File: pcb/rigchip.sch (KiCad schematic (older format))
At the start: 28 parts, among them IC1 TSR1, IC2 CHIPv1_0, J1 POWER, J2 DATA, J3 CONTROL

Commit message: first go at routing
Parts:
- J1: footprint (none) -> agg:S02B-PASK-2
- J2: footprint (none) -> agg:S05B-PASK-2
- J3: footprint (none) -> agg:S03B-PASK-2
- L1: value 5.6µ -> 6µ8; footprint (none) -> agg:TYS5040; Farnell (none) -> 2292530
- L2, L3, L4, L5, L6, L7: value L -> FB
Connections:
- net GND: now also IC2.L1 (GND)
- net at IC2.R15 (XIO-P2): now also R1.1
- net at IC2.R16 (XIO-P3): now also R2.1
- net at IC2.R19 (XIO-P6): no longer R1.1
- net at IC2.R20 (XIO-P7): no longer R2.1
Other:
- moved on the sheet: D8, D9, R1, R2

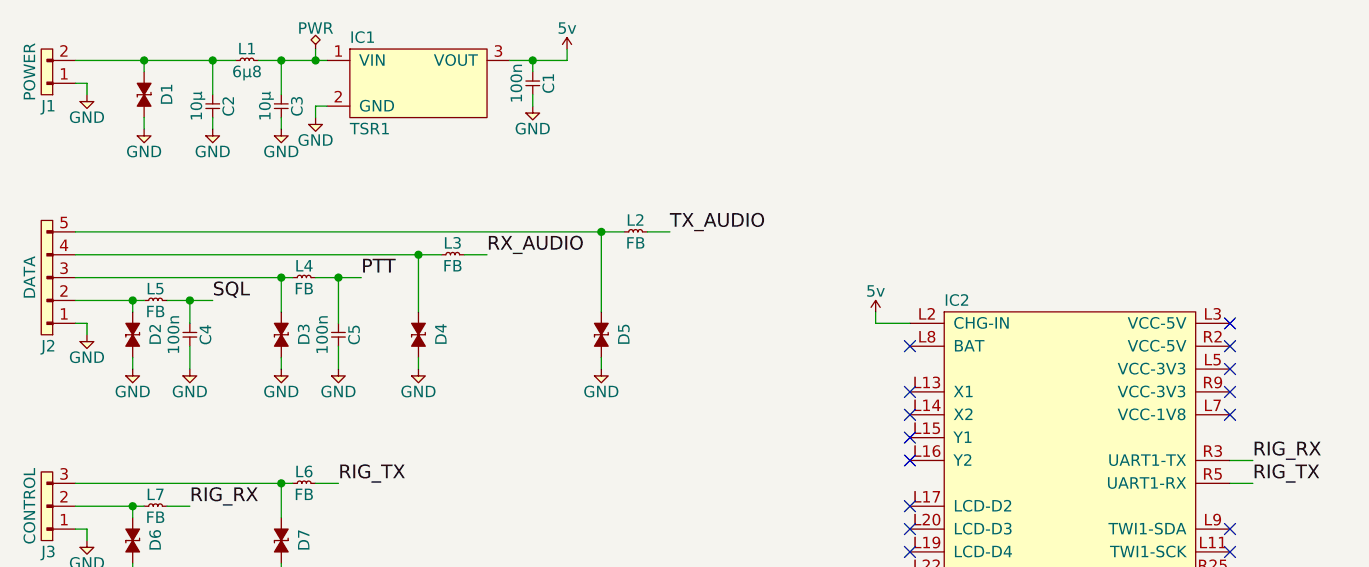
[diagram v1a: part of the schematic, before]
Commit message: reroute, no more tracks underneath and nice shielding
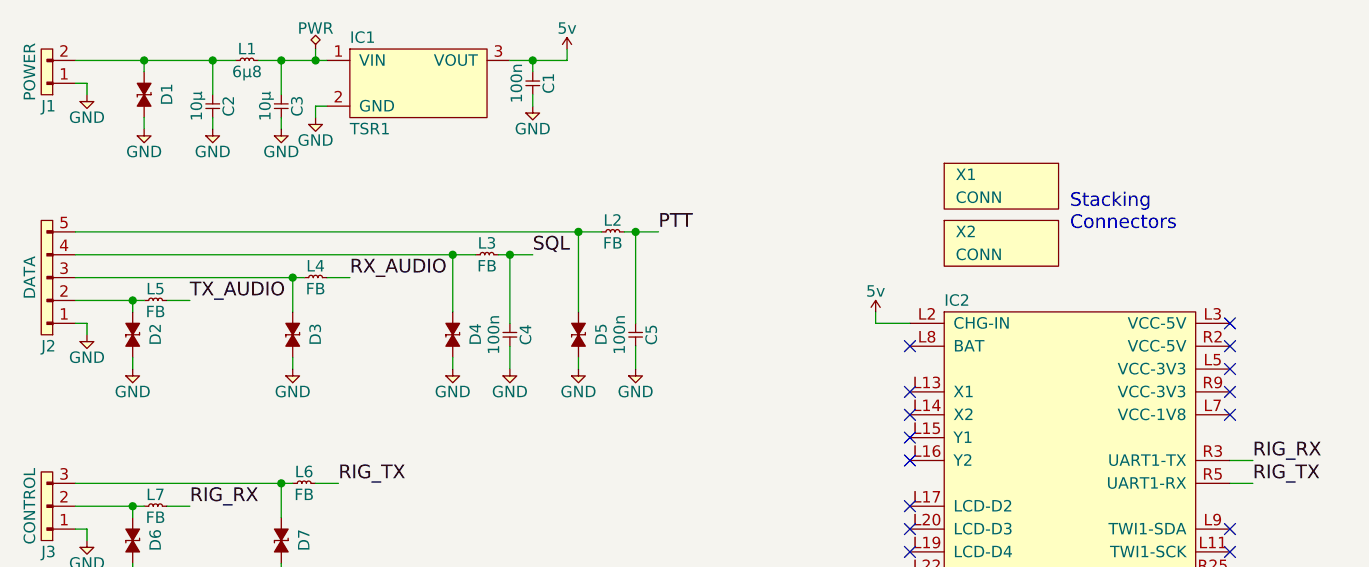
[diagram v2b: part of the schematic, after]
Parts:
- added X1, X2: CONN, symbol PART
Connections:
- net PTT: now also L2.2; no longer L4.2
- net RX_AUDIO: now also L4.2; no longer L3.2
- net SQL: now also L3.2; no longer L5.2
- net TX_AUDIO: now also L5.2; no longer L2.2
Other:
- note added: "Stacking\nConnectors"
- moved on the sheet: C4, C5, D3, D4, D5, L2, L3, L4
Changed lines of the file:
@@
 L ESD_DIODE D5
 U 1 1 56F7F170
-P 3450 2100
-F 0 "D5" H 3400 2200 50  0000 L CNN
-F 1 "ESD_DIODE" H 3400 2000 50  0001 L CNN
-F 2 "agg:0402" H 3400 1900 50  0001 L CNN
-F 3 "" H 3350 2100 50  0001 C CNN
-F 4 "2368169" H 3400 1800 50  0001 L CNN "Farnell"
-	1    3450 2100
+P 3350 2100
+F 0 "D5" H 3300 2200 50  0000 L CNN
+F 1 "ESD_DIODE" H 3300 2000 50  0001 L CNN
+F 2 "agg:0402" H 3300 1900 50  0001 L CNN
+F 3 "" H 3250 2100 50  0001 C CNN
+F 4 "2368169" H 3300 1800 50  0001 L CNN "Farnell"
+	1    3350 2100
 	0    1    1    0
 $EndComp
@@
 L ESD_DIODE D4
 U 1 1 56F7F1C6
-P 2650 2100
-F 0 "D4" H 2600 2200 50  0000 L CNN
-F 1 "ESD_DIODE" H 2600 2000 50  0001 L CNN
-F 2 "agg:0402" H 2600 1900 50  0001 L CNN
-F 3 "" H 2550 2100 50  0001 C CNN
-F 4 "2368169" H 2600 1800 50  0001 L CNN "Farnell"
-	1    2650 2100
+P 2800 2100
+F 0 "D4" H 2750 2200 50  0000 L CNN
+F 1 "ESD_DIODE" H 2750 2000 50  0001 L CNN
+F 2 "agg:0402" H 2750 1900 50  0001 L CNN
+F 3 "" H 2700 2100 50  0001 C CNN
+F 4 "2368169" H 2750 1800 50  0001 L CNN "Farnell"
+	1    2800 2100
 	0    1    1    0
 $EndComp
@@
 L ESD_DIODE D3
 U 1 1 56F7F1FF
-P 2050 2100
-F 0 "D3" H 2000 2200 50  0000 L CNN
-F 1 "ESD_DIODE" H 2000 2000 50  0001 L CNN
-F 2 "agg:0402" H 2000 1900 50  0001 L CNN
-F 3 "" H 1950 2100 50  0001 C CNN
-F 4 "2368169" H 2000 1800 50  0001 L CNN "Farnell"
-	1    2050 2100
+P 2100 2100
+F 0 "D3" H 2050 2200 50  0000 L CNN
+F 1 "ESD_DIODE" H 2050 2000 50  0001 L CNN
+F 2 "agg:0402" H 2050 1900 50  0001 L CNN
+F 3 "" H 2000 2100 50  0001 C CNN
+F 4 "2368169" H 2050 1800 50  0001 L CNN "Farnell"
+	1    2100 2100
 	0    1    1    0
 $EndComp
@@
 L C C4
 U 1 1 56F7F528
-P 1650 2050
-F 0 "C4" H 1700 2120 50  0000 C CNN
-F 1 "100n" H 1700 1980 50  0000 C CNN
-F 2 "agg:0603" H 1650 2050 50  0001 C CNN
-F 3 "" H 1650 2050 50  0001 C CNN
-	1    1650 2050
+P 3050 2050
+F 0 "C4" H 3100 2120 50  0000 C CNN
+F 1 "100n" H 3100 1980 50  0000 C CNN
+F 2 "agg:0603" H 3050 2050 50  0001 C CNN
+F 3 "" H 3050 2050 50  0001 C CNN
+	1    3050 2050
 	0    1    1    0
 $EndComp
@@
 L C C5
 U 1 1 56F7F59B
-P 2300 2050
-F 0 "C5" H 2350 2120 50  0000 C CNN
-F 1 "100n" H 2350 1980 50  0000 C CNN
-F 2 "agg:0603" H 2300 2050 50  0001 C CNN
-F 3 "" H 2300 2050 50  0001 C CNN
-	1    2300 2050
+P 3600 2050
+F 0 "C5" H 3650 2120 50  0000 C CNN
+F 1 "100n" H 3650 1980 50  0000 C CNN
+F 2 "agg:0603" H 3600 2050 50  0001 C CNN
+F 3 "" H 3600 2050 50  0001 C CNN
+	1    3600 2050
 	0    1    1    0
 $EndComp
@@
 L GND #PWR010
 U 1 1 56F826D2
-P 2050 2250
-F 0 "#PWR010" H 1920 2290 50  0001 L CNN
-F 1 "GND" H 2050 2150 50  0000 C CNN
-F 2 "" H 2050 2250 60  0000 C CNN
-F 3 "" H 2050 2250 60  0000 C CNN
-	1    2050 2250
+P 2100 2250
+F 0 "#PWR010" H 1970 2290 50  0001 L CNN
+F 1 "GND" H 2100 2150 50  0000 C CNN
+F 2 "" H 2100 2250 60  0000 C CNN
+F 3 "" H 2100 2250 60  0000 C CNN
+	1    2100 2250
 	1    0    0    -1
 $EndComp
@@
 L GND #PWR011
 U 1 1 56F82716
-P 2650 2250
-F 0 "#PWR011" H 2520 2290 50  0001 L CNN
-F 1 "GND" H 2650 2150 50  0000 C CNN
-F 2 "" H 2650 2250 60  0000 C CNN
-F 3 "" H 2650 2250 60  0000 C CNN
-	1    2650 2250
+P 2800 2250
+F 0 "#PWR011" H 2670 2290 50  0001 L CNN
+F 1 "GND" H 2800 2150 50  0000 C CNN
+F 2 "" H 2800 2250 60  0000 C CNN
+F 3 "" H 2800 2250 60  0000 C CNN
+	1    2800 2250
 	1    0    0    -1
 $EndComp
@@
 L GND #PWR012
 U 1 1 56F8275A
-P 3450 2250
-F 0 "#PWR012" H 3320 2290 50  0001 L CNN
-F 1 "GND" H 3450 2150 50  0000 C CNN
-F 2 "" H 3450 2250 60  0000 C CNN
-F 3 "" H 3450 2250 60  0000 C CNN
-	1    3450 2250
+P 3350 2250
+F 0 "#PWR012" H 3220 2290 50  0001 L CNN
+F 1 "GND" H 3350 2150 50  0000 C CNN
+F 2 "" H 3350 2250 60  0000 C CNN
+F 3 "" H 3350 2250 60  0000 C CNN
+	1    3350 2250
 	1    0    0    -1
 $EndComp
@@
 L GND #PWR013
 U 1 1 56F829A6
-P 1650 2250
-F 0 "#PWR013" H 1520 2290 50  0001 L CNN
-F 1 "GND" H 1650 2150 50  0000 C CNN
-F 2 "" H 1650 2250 60  0000 C CNN
-F 3 "" H 1650 2250 60  0000 C CNN
-	1    1650 2250
+P 3050 2250
+F 0 "#PWR013" H 2920 2290 50  0001 L CNN
+F 1 "GND" H 3050 2150 50  0000 C CNN
+F 2 "" H 3050 2250 60  0000 C CNN
+F 3 "" H 3050 2250 60  0000 C CNN
+	1    3050 2250
 	1    0    0    -1
 $EndComp
@@
 L GND #PWR014
 U 1 1 56F829EA
-P 2300 2250
-F 0 "#PWR014" H 2170 2290 50  0001 L CNN
-F 1 "GND" H 2300 2150 50  0000 C CNN
-F 2 "" H 2300 2250 60  0000 C CNN
-F 3 "" H 2300 2250 60  0000 C CNN
-	1    2300 2250
+P 3600 2250
+F 0 "#PWR014" H 3470 2290 50  0001 L CNN
+F 1 "GND" H 3600 2150 50  0000 C CNN
+F 2 "" H 3600 2250 60  0000 C CNN
+F 3 "" H 3600 2250 60  0000 C CNN
+	1    3600 2250
 	1    0    0    -1
 $EndComp
@@
 L L L4
 U 1 1 56F82B65
-P 2100 1850
-F 0 "L4" H 2150 1900 50  0000 C CNN
-F 1 "FB" H 2150 1800 50  0000 C CNN
-F 2 "agg:0603" H 2100 1850 50  0001 C CNN
-F 3 "" H 2100 1850 50  0001 C CNN
-	1    2100 1850
+P 2150 1850
+F 0 "L4" H 2200 1900 50  0000 C CNN
+F 1 "FB" H 2200 1800 50  0000 C CNN
+F 2 "agg:0603" H 2150 1850 50  0001 C CNN
+F 3 "" H 2150 1850 50  0001 C CNN
+	1    2150 1850
 	1    0    0    -1
 $EndComp
@@
 L L L3
 U 1 1 56F82BD1
-P 2750 1750
-F 0 "L3" H 2800 1800 50  0000 C CNN
-F 1 "FB" H 2800 1700 50  0000 C CNN
-F 2 "agg:0603" H 2750 1750 50  0001 C CNN
-F 3 "" H 2750 1750 50  0001 C CNN
-	1    2750 1750
+P 2900 1750
+F 0 "L3" H 2950 1800 50  0000 C CNN
+F 1 "FB" H 2950 1700 50  0000 C CNN
+F 2 "agg:0603" H 2900 1750 50  0001 C CNN
+F 3 "" H 2900 1750 50  0001 C CNN
+	1    2900 1750
 	1    0    0    -1
 $EndComp
@@
 L L L2
 U 1 1 56F82C32
-P 3550 1650
-F 0 "L2" H 3600 1700 50  0000 C CNN
-F 1 "FB" H 3600 1600 50  0000 C CNN
-F 2 "agg:0603" H 3550 1650 50  0001 C CNN
-F 3 "" H 3550 1650 50  0001 C CNN
-	1    3550 1650
-	1    0    0    -1
-$EndComp
-Text Label 1750 1950 0    60   ~ 0
+P 3450 1650
+F 0 "L2" H 3500 1700 50  0000 C CNN
+F 1 "FB" H 3500 1600 50  0000 C CNN
+F 2 "agg:0603" H 3450 1650 50  0001 C CNN
+F 3 "" H 3450 1650 50  0001 C CNN
+	1    3450 1650
+	1    0    0    -1
+$EndComp
+Text Label 3150 1750 0    60   ~ 0
 SQL
-Text Label 2400 1850 0    60   ~ 0
+Text Label 3700 1650 0    60   ~ 0
 PTT
-Text Label 2950 1750 0    60   ~ 0
+Text Label 2350 1850 0    60   ~ 0
 RX_AUDIO
-Text Label 3750 1650 0    60   ~ 0
+Text Label 1650 1950 0    60   ~ 0
 TX_AUDIO
 $Comp
@@
 Connection ~ 1400 1950
 Wire Wire Line
-	1550 1950 1750 1950
-Wire Wire Line
-	1650 1950 1650 2050
-Wire Wire Line
-	1650 2150 1650 2250
+	3050 1750 3050 2050
+Wire Wire Line
+	3050 2150 3050 2250
 Wire Wire Line
 	1400 2200 1400 2250
-Connection ~ 1650 1950
-Wire Wire Line
-	1150 1850 2100 1850
-Wire Wire Line
-	2050 1850 2050 2000
-Connection ~ 2050 1850
-Wire Wire Line
-	2050 2200 2050 2250
-Wire Wire Line
-	2300 2250 2300 2150
-Wire Wire Line
-	2200 1850 2400 1850
-Wire Wire Line
-	2300 1850 2300 2050
-Connection ~ 2300 1850
-Wire Wire Line
-	1150 1750 2750 1750
-Wire Wire Line
-	2650 2200 2650 2250
-Wire Wire Line
-	3450 2200 3450 2250
-Wire Wire Line
-	1150 1650 3550 1650
+Wire Wire Line
+	1150 1850 2150 1850
+Wire Wire Line
+	2100 1850 2100 2000
+Connection ~ 2100 1850
+Wire Wire Line
+	2100 2200 2100 2250
+Wire Wire Line
+	3600 2250 3600 2150
+Wire Wire Line
+	3600 1650 3600 2050
+Wire Wire Line
+	1150 1750 2900 1750
+Wire Wire Line
+	2800 2200 2800 2250
+Wire Wire Line
+	3350 2200 3350 2250
 Wire Wire Line
 	1150 2950 1200 2950
@@
 	1400 2850 1400 2900
 Wire Wire Line
-	2650 1750 2650 2000
-Connection ~ 2650 1750
-Wire Wire Line
-	2850 1750 2950 1750
-Wire Wire Line
-	3450 1650 3450 2000
-Connection ~ 3450 1650
-Wire Wire Line
-	3750 1650 3650 1650
+	2800 1750 2800 2000
+Connection ~ 2800 1750
+Wire Wire Line
+	3000 1750 3150 1750
+Wire Wire Line
+	3350 1650 3350 2000
+Connection ~ 3350 1650
+Wire Wire Line
+	3550 1650 3700 1650
 Connection ~ 1400 2850
 Wire Wire Line
@@
 NoConn ~ 6200 4050
 NoConn ~ 6200 4150
+$Comp
+L PART X1
+U 1 1 56F82D3C
+P 4950 1500
+F 0 "X1" H 5000 1600 50  0000 L CNN
+F 1 "CONN" H 5000 1500 50  0000 L CNN
+F 2 "" H 4950 1500 50  0001 C CNN
+F 3 "" H 4950 1500 50  0001 C CNN
+F 4 "1569230" H 4950 1500 60  0001 C CNN "Farnell"
+	1    4950 1500
+	1    0    0    -1
+$EndComp
+$Comp
+L PART X2
+U 1 1 56F82E20
+P 4950 1750
+F 0 "X2" H 5000 1850 50  0000 L CNN
+F 1 "CONN" H 5000 1750 50  0000 L CNN
+F 2 "" H 4950 1750 50  0001 C CNN
+F 3 "" H 4950 1750 50  0001 C CNN
+F 4 "1569230" H 4950 1750 60  0001 C CNN "Farnell"
+	1    4950 1750
+	1    0    0    -1
+$EndComp
+Text Notes 5500 1650 0    60   ~ 0
+Stacking\nConnectors
+Wire Wire Line
+	1550 1950 1650 1950
+Wire Wire Line
+	2350 1850 2250 1850
+Connection ~ 3050 1750
+Wire Wire Line
+	1150 1650 3450 1650
+Connection ~ 3600 1650
 $EndSCHEMATC

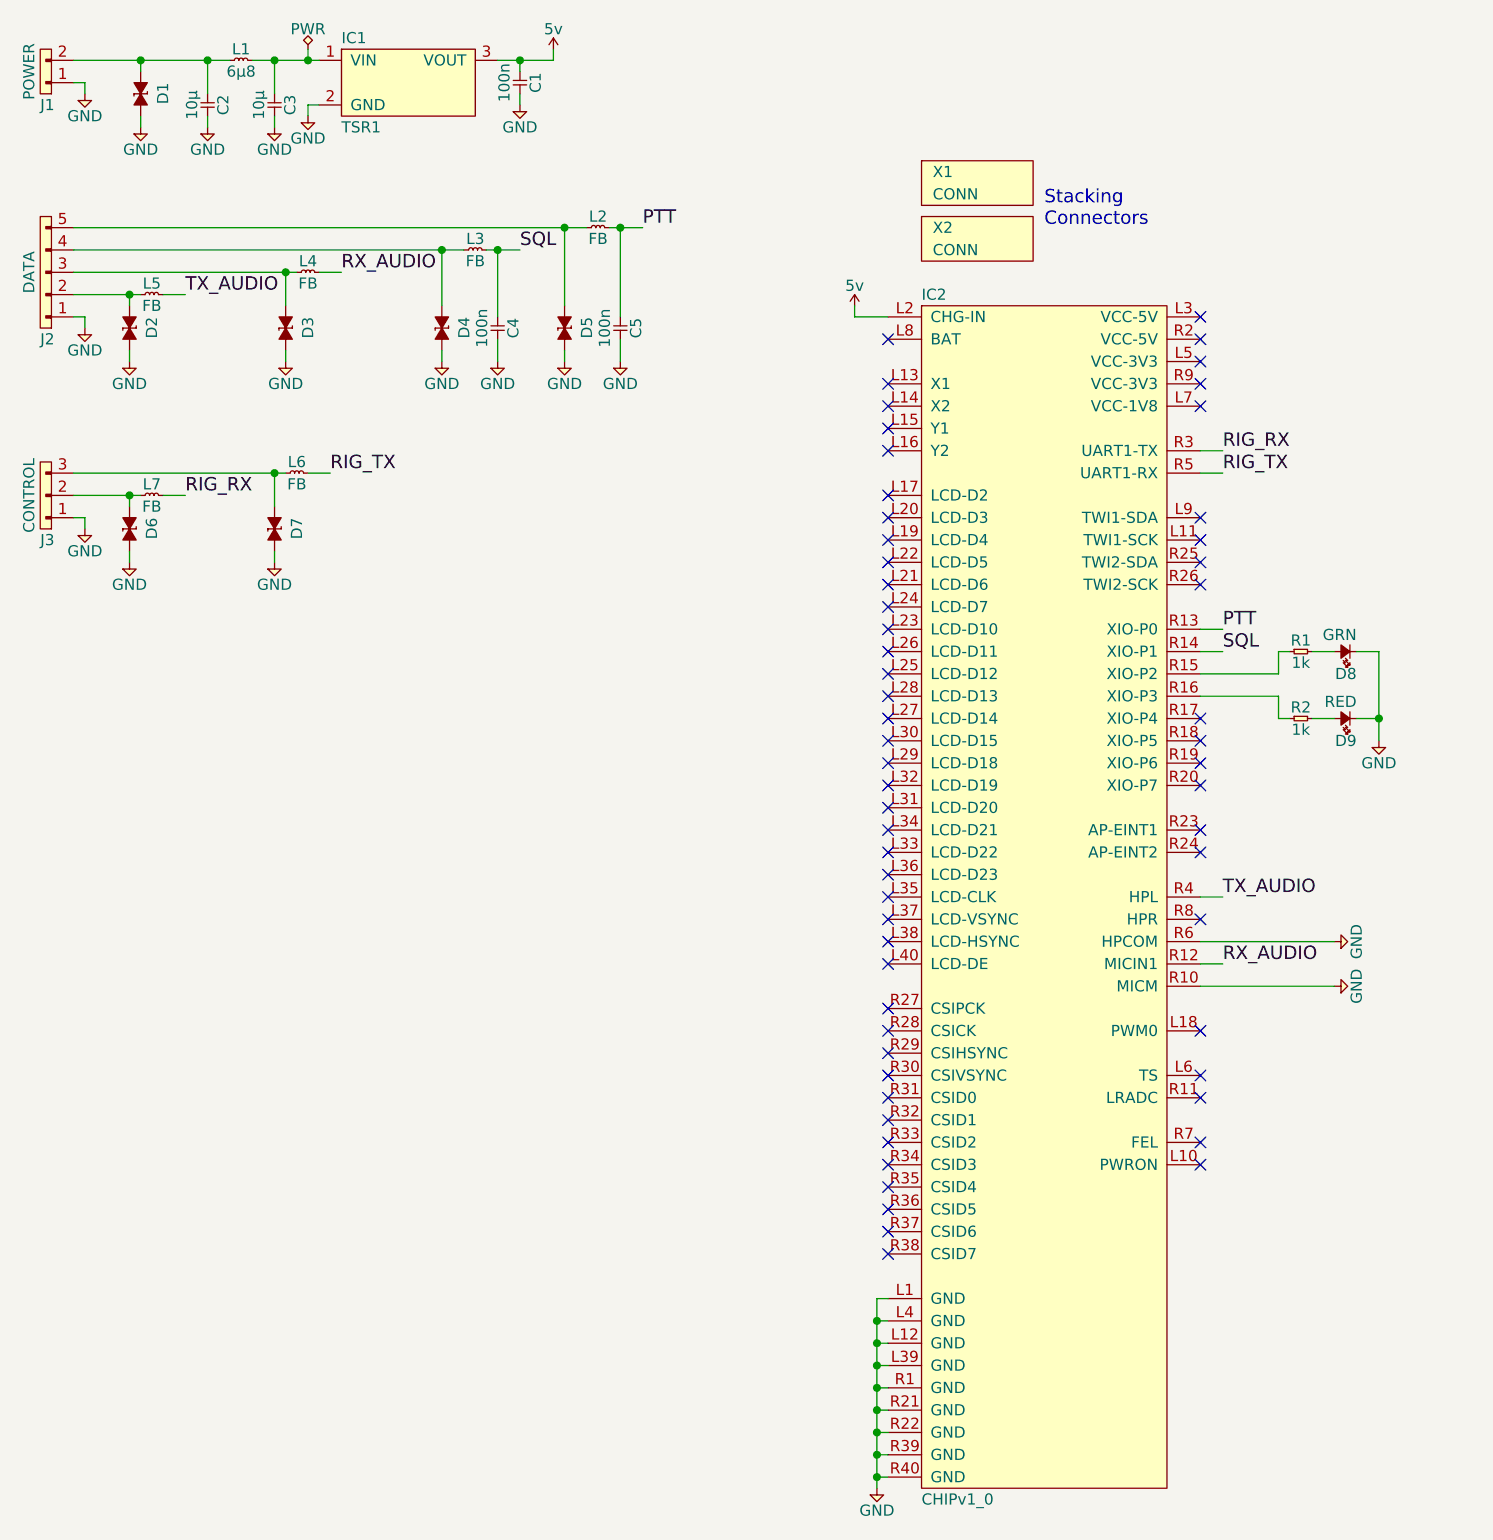
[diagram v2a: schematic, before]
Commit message: add buffers to cat control
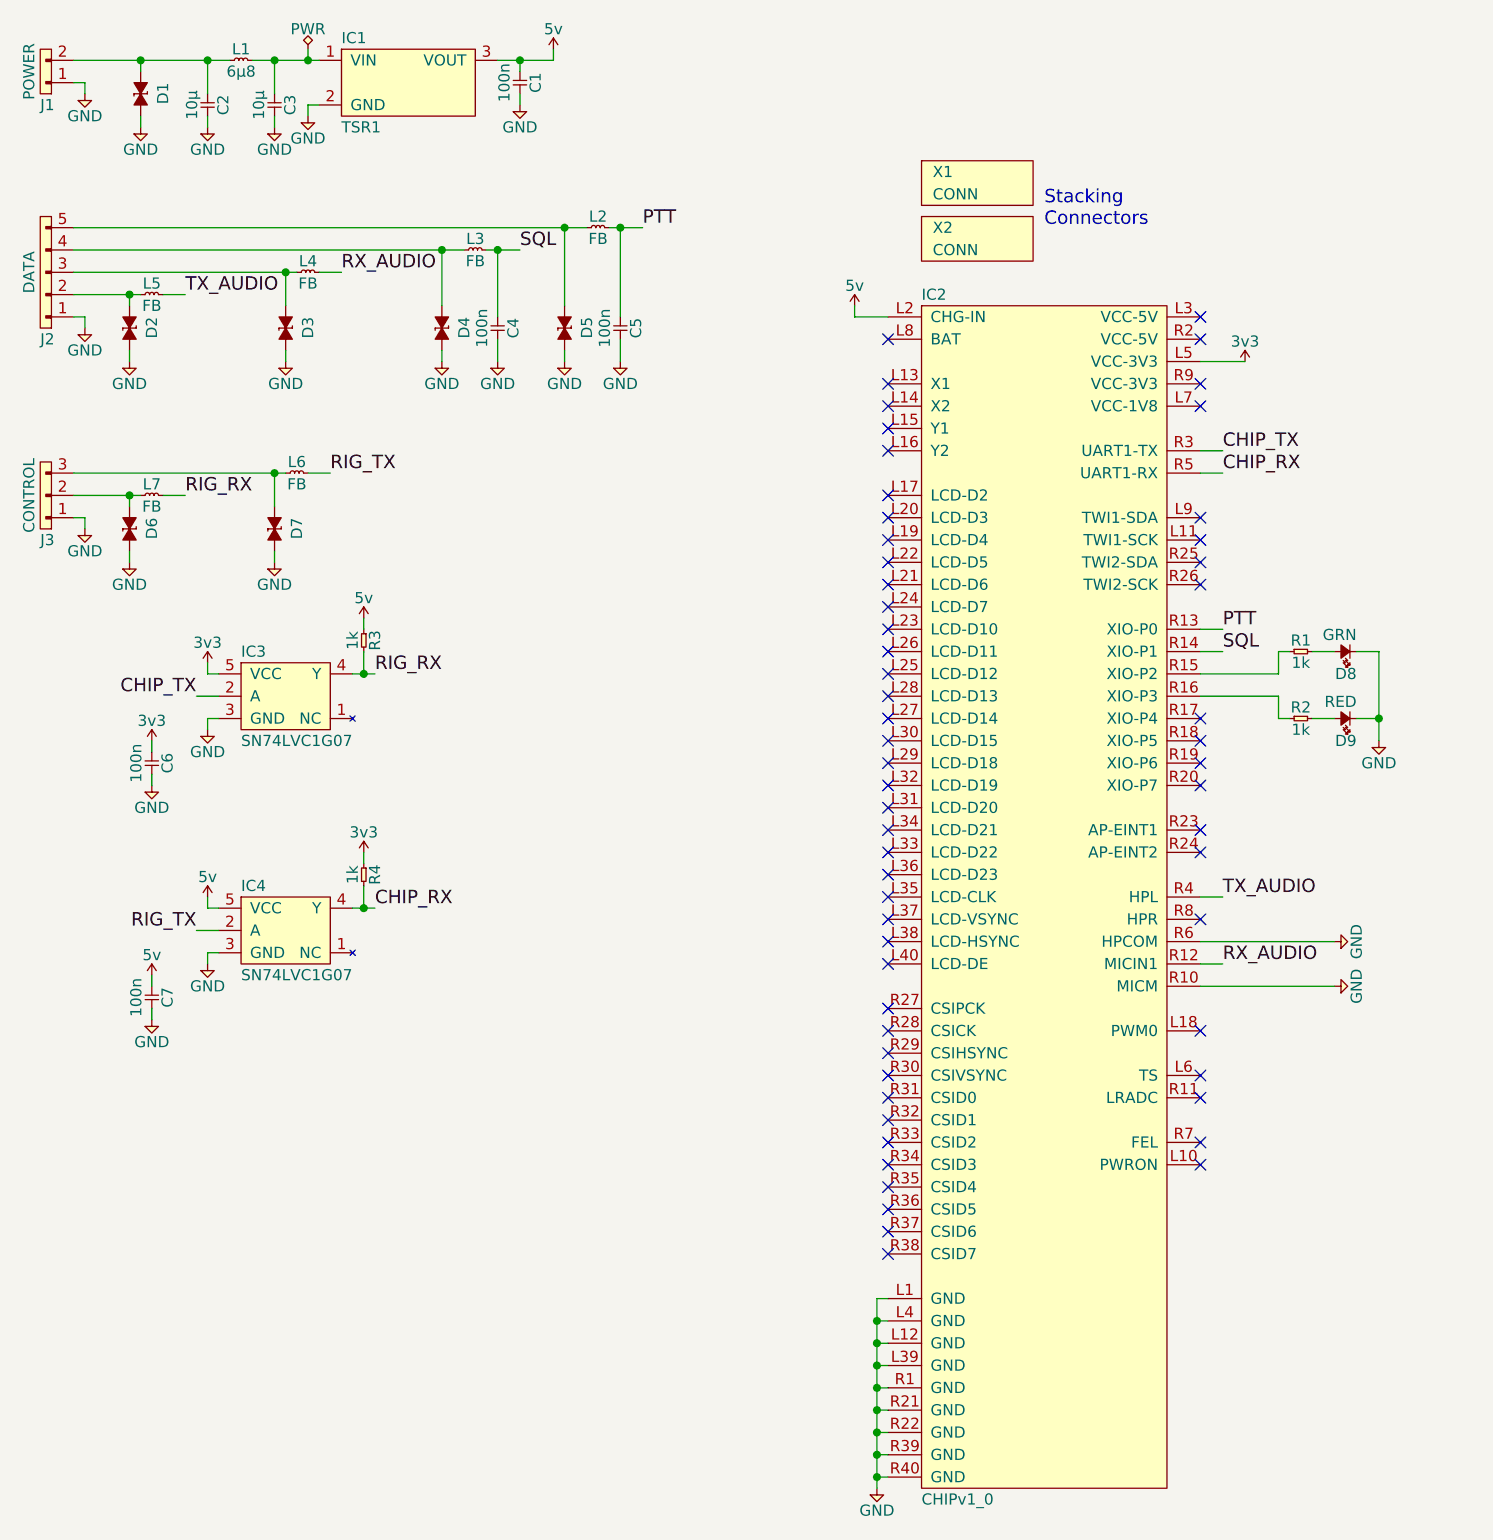
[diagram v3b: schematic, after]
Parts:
- added C6, C7: 100n, agg:0603, symbol C
- added IC3, IC4: SN74LVC1G07, agg:SOT-23-5, symbol SN74LVC1G07
- added R3, R4: 1k, agg:0603, symbol R
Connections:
- net 5v: now also C7.1, IC4.5 (VCC), R3.1
- net GND: now also C6.2, C7.2, IC3.3 (GND), IC4.3 (GND)
- net RIG_RX: now also IC3.4 (Y), R3.2; no longer IC2.R3 (UART1-TX)
- net RIG_TX: now also IC4.2 (A); no longer IC2.R5 (UART1-RX)
- net 3v3: now reaches IC2.L5 (VCC-3V3)
- net 3v3: now also C6.1, IC3.5 (VCC), R4.1
- new net CHIP_RX: IC2.R5 (UART1-RX), IC4.4 (Y), R4.2
- new net CHIP_TX: IC2.R3 (UART1-TX), IC3.2 (A)
- no-connect marks 60 -> 59
